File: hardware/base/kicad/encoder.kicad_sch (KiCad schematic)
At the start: 44 parts, among them J10 ENCODER, U21 TPS1H000AQDGNRQ1, U22 AM26LV32EIDR

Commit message: Accept a 12 V or 24 V supply on the base board (10.8 to 30 V)
- Supply nets renamed +VIN and +VIN_OUT (silkscreen VIN OUT).
- UVLO 200 k over 47 k // 100 k: start 8.47 V (9.48 V worst case),
  stop 7.79 V; fuse 3.5 A (12H1350C).
- 0-10 V: OPA2990 rail-to-rail op amp supplied by +VIN, SS8550 current
  limit across the 120 ohm; 10 V into 10 k from 10.9 V of supply.
- E-stop and probe inputs: 2 x 4.7 k in parallel, shunts 1 k and 4.7 k.
- Buck simulated from 7.8 to 30 V with the smallest slope compensation
  the datasheet allows: 79 deg, 11.6 dB minimum.
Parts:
- JP1: value ENC 5V|24V -> ENC 5V|VIN
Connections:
- net +24V renamed +VIN
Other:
- note added: "Shunt 1-2: 5 V, 2-3: VIN (12 or 24 V), none: no supply. 218 mA limit."
- note removed: "Shunt 1-2: 5 V, 2-3: 24 V, none: no supply. 218 mA limit."
- title: Encoder port: RS-422, TTL or HTL, 5 V or 24 V (4 instances) -> Encoder port: RS-422, TTL or HTL, 5 V or VIN (4 instances)
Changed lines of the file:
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@@
 	(paper "A3")
 	(title_block
-		(title "Encoder port: RS-422, TTL or HTL, 5 V or 24 V (4 instances)")
+		(title "Encoder port: RS-422, TTL or HTL, 5 V or VIN (4 instances)")
 		(date "2026-10-18")
 		(rev "A")

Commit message: Trim the base board BOM: 60 to 58 lines
- ESD of NRST and of the PWM output on one channel of the TPD4E05U06
  already used on the PHY lines, instead of a PESD5V0S1BA.
- SS56B instead of SS34 for the 5 V / USB OR-ing and the encoder
  supplies.
- One 100 uF 10 V X5R 1210 on the 5 V buck output instead of two 47 uF:
  about 55 uF at 5 V, inside the simulated 34-80 uF.
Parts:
- D28: value SS34 -> SS56B; footprint Diode_SMD:D_SMA -> Diode_SMD:D_SMB; LCSC C8678 -> C14651

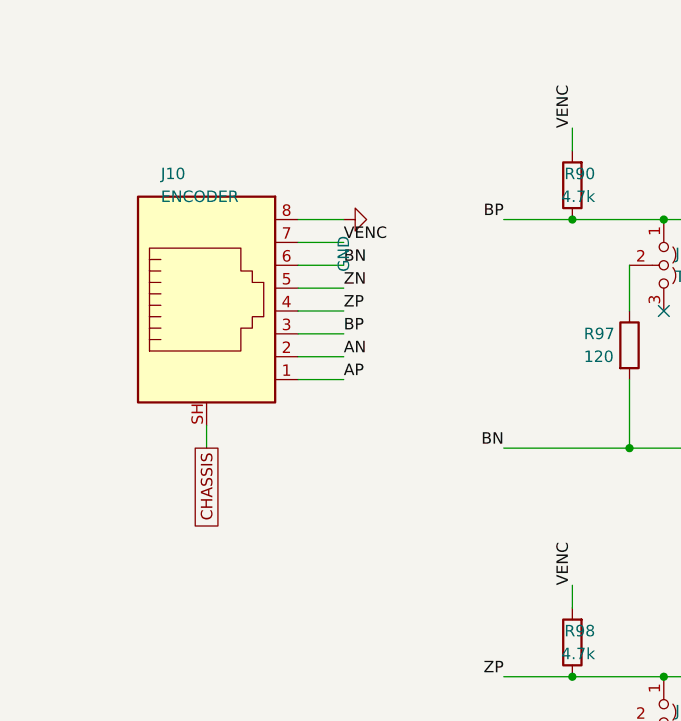
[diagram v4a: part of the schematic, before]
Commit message: Start the base board PCB: outline, profile rules, connectors on the edges
- pcb.py builds the board from the schematic: 72 x 150 mm, 4 layers,
  C-LOCK keyhole, M3 holes, connectors on both long edges; the other
  parts are parked beside the board until they are placed.
- base.kicad_dru: rules of the Phoenix UM-BASIC 72 profile (no part at
  the short edges on the top side, no through-hole lead on the rim the
  board rests on), proved by the DRC.
- Dual shielded RJ45 per axis (HC-WK88-H132-1X2-55B): port A for the
  drive, port B for the encoder. kicadgen draws multi-unit symbols, one
  unit per sheet; footprint and 3D model generated from the datasheet.
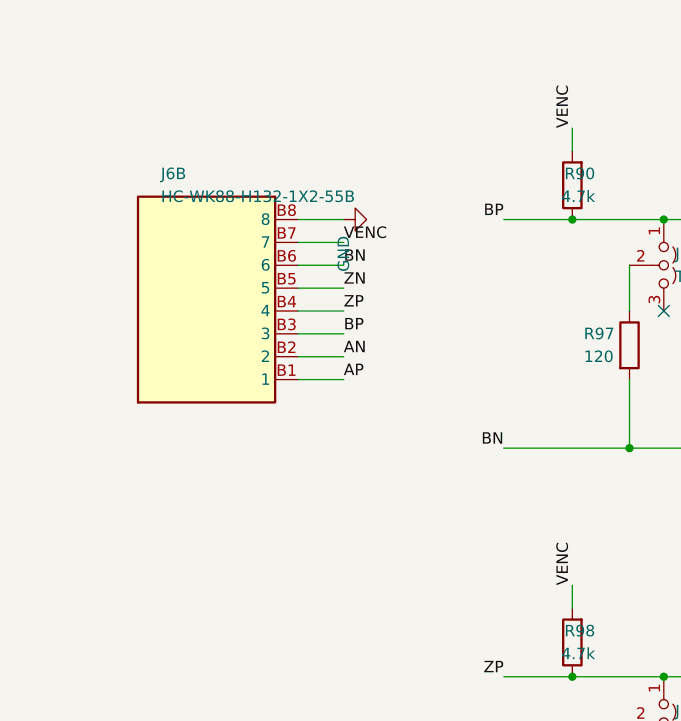
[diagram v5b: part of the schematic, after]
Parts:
- removed J10: ENCODER, Bornier:RJ45_HOAUC_HYCW48-RJ45-163B, symbol Connector:RJ45_Shielded
- added J6: HC-WK88-H132-1X2-55B, Bornier:RJ45x2_HongCheng_HC-WK88-H132-1X2-55B, symbol Bornier:RJ45x2_Shielded
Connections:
- net AN: now also J6.B2 (2)
- net AP: now also J6.B1 (1)
- net BN: now also J6.B6 (6)
- net BP: now also J6.B3 (3)
- net GND: now also J6.B8 (8)
- net VENC: now also J6.B7 (7)
- net ZN: now also J6.B5 (5)
- net ZP: now also J6.B4 (4)

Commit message: Place the base board parts; DIP switches for the encoder terminations
Placement (gen/pcb.py): one zone per schematic sheet, key parts placed by
hand, the other parts next to the pin they serve, bulkiest first, with a
1 mm gap preferred when it costs at most 2 mm. The local bus header stands
at the left end, centred across the board, facing the modules.

Encoder terminations: one CTS 218-4LPSTR DIP switch per encoder (100 mA
non-switching) replaces three SMD jumpers; the supply selector and the
Modbus termination use a through-hole 1x3 header. Split DIP symbol, one
unit per switch, drawn on the pair it serves.

DRC rules: 0.2 mm thermal vias, per-package clearance for 0.65 mm pitch
parts. Test points out of the BOM, DNP copied to the footprints. pcb.py
keeps the schematic settings of the project file and finds the KiCad
footprint libraries on every install.

Claude-Session: https://claude.ai/code/session_01JfmMsHNpEd1mfzHNWc4koJ
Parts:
- removed JP2, JP3, JP4: TERM, Bornier:PinHeader_1x03_P2.54mm_Vertical_SMD_HX_PZ254, symbol Jumper:Jumper_3_Open
- added SW2: TERM A B Z, Button_Switch_SMD:SW_DIP_SPSTx04_Slide_KingTek_DSHP04TS_W7.62mm_P1.27mm, symbol Bornier:SW_DIP_x04_Split
- JP1: footprint Bornier:PinHeader_1x03_P2.54mm_Vertical_SMD_HX_PZ254 -> Connector_PinHeader_2.54mm:PinHeader_1x03_P2.54mm_Vertical; LCSC C41417360 -> C2937625
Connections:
- net AP: now also SW2.1
- net BP: now also SW2.2
- net ZP: now also SW2.3
- net at R97.1: now also SW2.7
- net at R89.1: now also SW2.8
- net at R105.1: now also SW2.6
- no-connect marks 7 -> 6
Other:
- note added: "Placed four times (encoders 0 to 3). Per line: 3.3 k series, Schottky clamp to 0..5 V, bias 4.7 k / 4.7 k at the receiver: an open line sits at 2.5 V, so a single-ended encoder (TTL, HTL, open collector) works with its - line unconnected. + lines pulled up to the encoder supply. TERM switches: on for RS-422 only, set with the encoder off."
- note added: "Spare"
- note removed: "Placed four times (encoders 0 to 3). Per line: 3.3 k series, Schottky clamp to 0..5 V, bias 4.7 k / 4.7 k at the receiver: an open line sits at 2.5 V, so a single-ended encoder (TTL, HTL, open collector) works with its - line unconnected. + lines pulled up to the encoder supply. TERM jumpers: shunt on 1-2 for RS-422 only, parked on 2-3 otherwise."
